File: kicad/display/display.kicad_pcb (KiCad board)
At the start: 2 copper layers, 190.5 x 38.1 mm, 27 parts, among them J10 Conn. 02x12, P1 10k, P2 10k, P3 10k stereo, P4 10k, T7 2N3904, T8 2N3904, U3 4066N

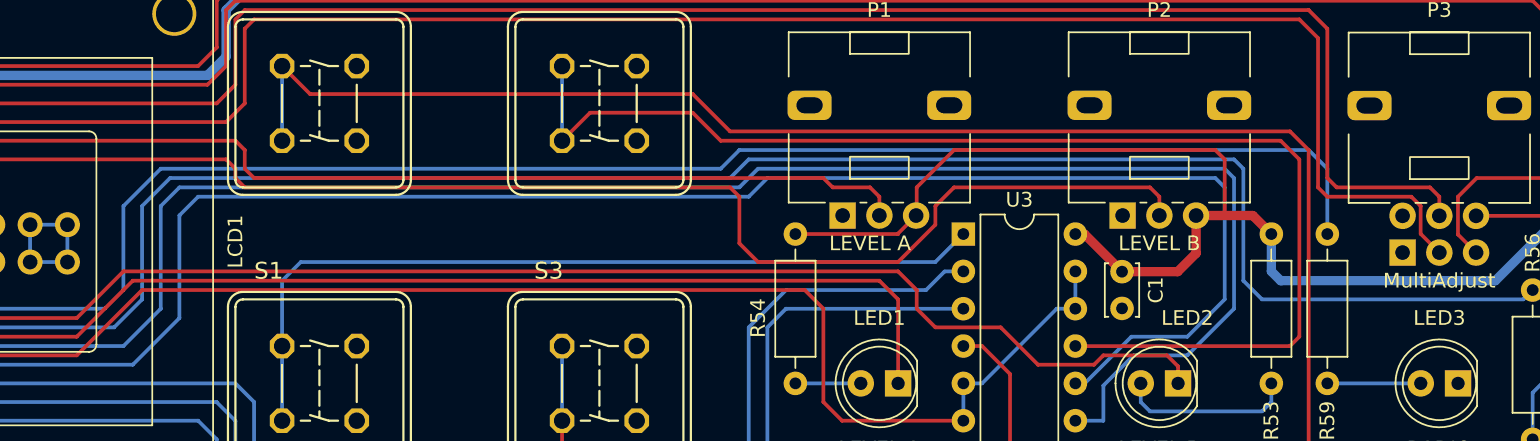
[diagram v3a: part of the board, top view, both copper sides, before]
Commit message: Cleaning up F.Fab layer, putting values at the right places.
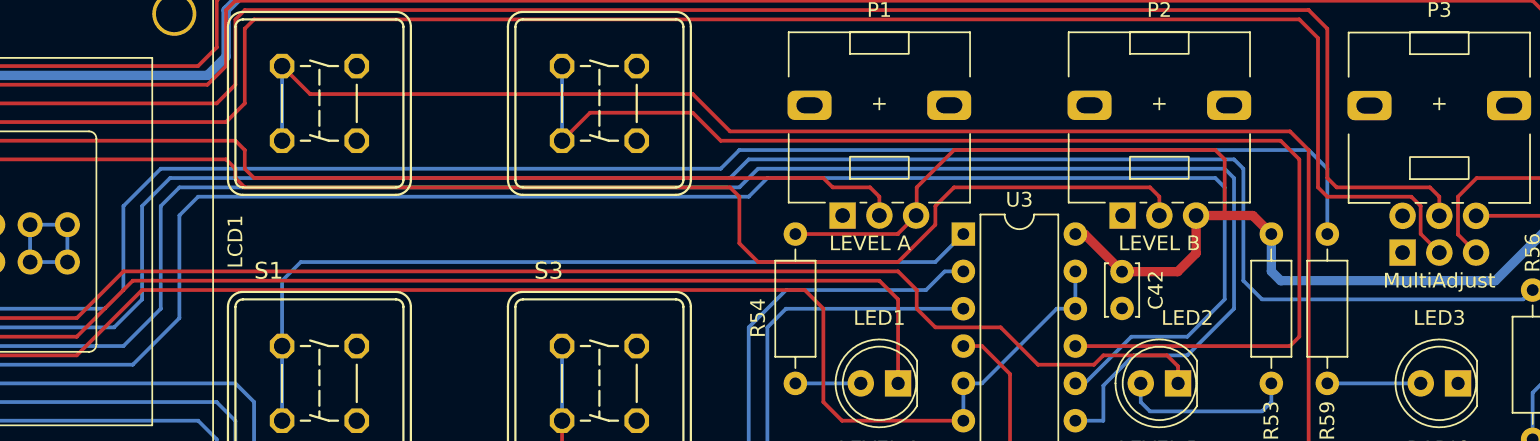
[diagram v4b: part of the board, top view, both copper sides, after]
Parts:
- renumbered C1 to C42
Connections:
- P1 pad MP: (no net) -> GND
- P2 pad MP: (no net) -> GND
- P3 pad MP: (no net) -> GND
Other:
- board text added: "+"
- board text removed: "16V"
- board text removed: "25V"
- board text removed: "6.3V"

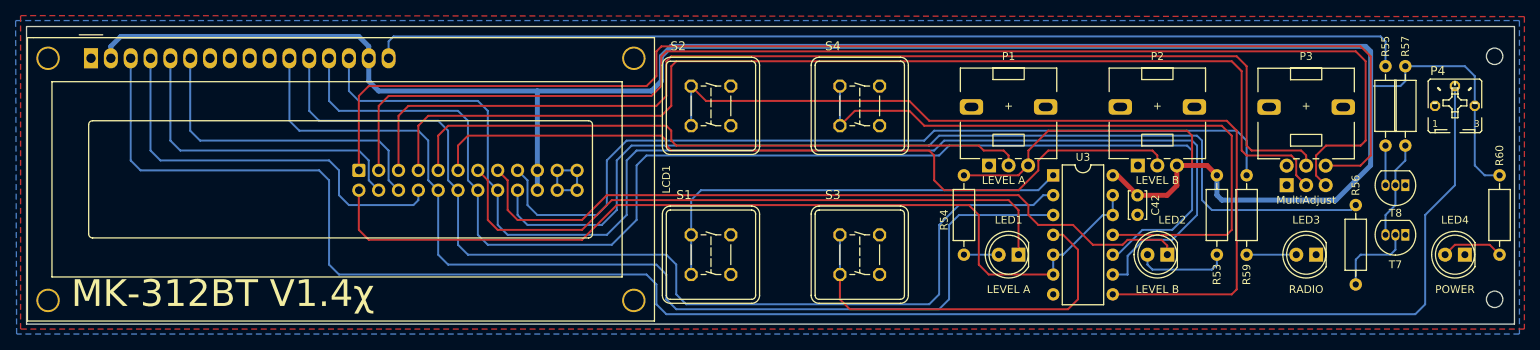
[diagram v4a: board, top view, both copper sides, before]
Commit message: Two small fixups for the display & frontend. Made mounting holes in display PCB larger. Moved LCD window slightly to the right on the front panel.
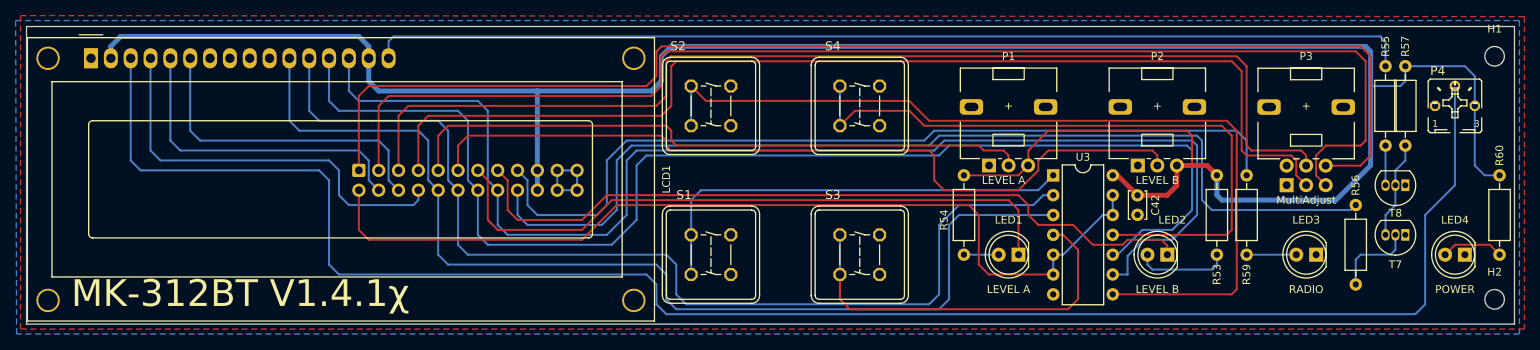
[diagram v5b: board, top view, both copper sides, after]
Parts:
- H1, H2: footprint MountingHole:MountingHole_2.1mm -> MountingHole:MountingHole_2.5mm
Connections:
- P1 pad MP: GND -> (no net)
- P2 pad MP: GND -> (no net)
- P3 pad MP: GND -> (no net)
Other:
- board text added: "MK-312BT V1.4.1χ"
- board text removed: "MK-312BT V1.4χ"
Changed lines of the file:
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@@
   (title_block
     (title "MK312BT Display Print")
-    (date "2022-08-01")
-    (rev "1.3.1-Chi")
+    (date "2022-09-05")
+    (rev "1.4.1-Chi")
   )
   (layers
@@
     )
   )
-  (footprint "MountingHole:MountingHole_2.1mm" (layer "F.Cu")
+  (footprint "MountingHole:MountingHole_2.5mm" (layer "F.Cu")
     (at 238.76 54.61)
-    (descr "Mounting Hole 2.1mm, no annular")
-    (tags "mounting hole 2.1mm no annular")
+    (descr "Mounting Hole 2.5mm, no annular")
+    (tags "mounting hole 2.5mm no annular")
     (property "Sheetfile" "display.kicad_sch")
     (property "Sheetname" "")
     (attr exclude_from_pos_files)
-    (fp_text reference "H1" (at 0 3.175) (layer "F.SilkS") hide
-      (effects (font (size 1 1) (thickness 0.15)))
-    )
-    (fp_text value "MountingHole topright" (at 0 3.2) (layer "F.Fab")
+    (fp_text reference "H1" (at 0 -3.5) (layer "F.SilkS")
+      (effects (font (size 1 1) (thickness 0.15)))
+    )
+    (fp_text value "MountingHole topright" (at 0 3.5) (layer "F.Fab") hide
       (effects (font (size 1 1) (thickness 0.15)))
     )
@@
       (effects (font (size 1 1) (thickness 0.15)))
     )
-    (fp_circle (center 0 0) (end 2.1 0) (layer "Cmts.User") (width 0.15) (fill none))
-    (fp_circle (center 0 0) (end 2.35 0) (layer "F.CrtYd") (width 0.05) (fill none))
-    (pad "" np_thru_hole circle (at 0 0) (size 2.1 2.1) (drill 2.1) (layers *.Cu *.Mask))
+    (fp_circle (center 0 0) (end 2.5 0) (layer "Cmts.User") (width 0.15) (fill none))
+    (fp_circle (center 0 0) (end 2.75 0) (layer "F.CrtYd") (width 0.05) (fill none))
+    (pad "" np_thru_hole circle (at 0 0) (size 2.5 2.5) (drill 2.5) (layers *.Cu *.Mask))
   )
   (footprint "Resistor_THT:R_Axial_DIN0207_L6.3mm_D2.5mm_P10.16mm_Horizontal" (layer "F.Cu")
@@
     (pad "3" thru_hole circle (at 0 5 90) (size 1.8 1.8) (drill 1) (layers *.Cu *.Mask)
       (net 27 "+5V") (pinfunction "3") (pintype "passive"))
-    (pad "MP" thru_hole roundrect (at 7.500011 7.249998 90) (size 2 2.999999) (drill oval 1.1 1.8) (layers *.Cu *.Mask) (roundrect_rratio 0.25)
-      (net 2 "GND"))
-    (pad "MP" thru_hole roundrect (at 7.500011 -2.250008 90) (size 2 2.999999) (drill oval 1.1 1.8) (layers *.Cu *.Mask) (roundrect_rratio 0.25)
-      (net 2 "GND"))
+    (pad "MP" thru_hole roundrect (at 7.500011 7.249998 90) (size 2 2.999999) (drill oval 1.1 1.8) (layers *.Cu *.Mask) (roundrect_rratio 0.25))
+    (pad "MP" thru_hole roundrect (at 7.500011 -2.250008 90) (size 2 2.999999) (drill oval 1.1 1.8) (layers *.Cu *.Mask) (roundrect_rratio 0.25))
     (zone (net 0) (net_name "") (layer "F.Cu") (name "Copper Keep Out") (hatch full 0.508)
       (connect_pads (clearance 0))
       (min_thickness 0.254)
-      (keepout (tracks not_allowed) (vias not_allowed) (pads not_allowed ) (copperpour not_allowed) (footprints not_allowed))
+      (keepout (tracks not_allowed) (vias not_allowed) (pads not_allowed) (copperpour not_allowed) (footprints not_allowed))
       (fill (thermal_gap 0.508) (thermal_bridge_width 0.508))
       (polygon
@@
       (connect_pads (clearance 0))
       (min_thickness 0.254)
-      (keepout (tracks not_allowed) (vias not_allowed) (pads not_allowed ) (copperpour not_allowed) (footprints not_allowed))
+      (keepout (tracks not_allowed) (vias not_allowed) (pads not_allowed) (copperpour not_allowed) (footprints not_allowed))
       (fill (thermal_gap 0.508) (thermal_bridge_width 0.508))
       (polygon
@@
     )
   )
-  (footprint "MountingHole:MountingHole_2.1mm" (layer "F.Cu")
+  (footprint "MountingHole:MountingHole_2.5mm" (layer "F.Cu")
     (at 238.76 85.725)
-    (descr "Mounting Hole 2.1mm, no annular")
-    (tags "mounting hole 2.1mm no annular")
+    (descr "Mounting Hole 2.5mm, no annular")
+    (tags "mounting hole 2.5mm no annular")
     (property "Sheetfile" "display.kicad_sch")
     (property "Sheetname" "")
     (attr exclude_from_pos_files)
-    (fp_text reference "H2" (at 0 -3.199994) (layer "F.SilkS") hide
-      (effects (font (size 1 1) (thickness 0.15)))
-    )
-    (fp_text value "MountingHole bottomright" (at 0 3.2) (layer "F.Fab")
+    (fp_text reference "H2" (at 0 -3.5) (layer "F.SilkS")
+      (effects (font (size 1 1) (thickness 0.15)))
+    )
+    (fp_text value "MountingHole bottomright" (at 0 3.5) (layer "F.Fab") hide
       (effects (font (size 1 1) (thickness 0.15)))
     )
@@
       (effects (font (size 1 1) (thickness 0.15)))
     )
-    (fp_circle (center 0 0) (end 2.1 0) (layer "Cmts.User") (width 0.15) (fill none))
-    (fp_circle (center 0 0) (end 2.35 0) (layer "F.CrtYd") (width 0.05) (fill none))
-    (pad "" np_thru_hole circle (at 0 0) (size 2.1 2.1) (drill 2.1) (layers *.Cu *.Mask))
+    (fp_circle (center 0 0) (end 2.5 0) (layer "Cmts.User") (width 0.15) (fill none))
+    (fp_circle (center 0 0) (end 2.75 0) (layer "F.CrtYd") (width 0.05) (fill none))
+    (pad "" np_thru_hole circle (at 0 0) (size 2.5 2.5) (drill 2.5) (layers *.Cu *.Mask))
   )
   (footprint "Potentiometer_THT:Potentiometer_Alps_RK09L_Double_Vertical" (layer "F.Cu")
@@
     (pad "6" thru_hole circle (at 2.5 5 90) (size 1.8 1.8) (drill 1) (layers *.Cu *.Mask)
       (net 1 "Net-(J10-Pad1)") (pinfunction "6") (pintype "passive"))
-    (pad "MP" thru_hole roundrect (at 10.000005 -2.250008 90) (size 2 2.999999) (drill oval 1.1 1.8) (layers *.Cu *.Mask) (roundrect_rratio 0.25)
-      (net 2 "GND"))
-    (pad "MP" thru_hole roundrect (at 10.000005 7.249998 90) (size 2 2.999999) (drill oval 1.1 1.8) (layers *.Cu *.Mask) (roundrect_rratio 0.25)
-      (net 2 "GND"))
+    (pad "MP" thru_hole roundrect (at 10.000005 -2.250008 90) (size 2 2.999999) (drill oval 1.1 1.8) (layers *.Cu *.Mask) (roundrect_rratio 0.25))
+    (pad "MP" thru_hole roundrect (at 10.000005 7.249998 90) (size 2 2.999999) (drill oval 1.1 1.8) (layers *.Cu *.Mask) (roundrect_rratio 0.25))
     (zone (net 0) (net_name "") (layer "F.Cu") (name "Copper Keep Out") (hatch full 0.508)
       (connect_pads (clearance 0))
       (min_thickness 0.254)
-      (keepout (tracks not_allowed) (vias not_allowed) (pads not_allowed ) (copperpour not_allowed) (footprints not_allowed))
+      (keepout (tracks not_allowed) (vias not_allowed) (pads not_allowed) (copperpour not_allowed) (footprints not_allowed))
       (fill (thermal_gap 0.508) (thermal_bridge_width 0.508))
       (polygon
@@
       (connect_pads (clearance 0))
       (min_thickness 0.254)
-      (keepout (tracks not_allowed) (vias not_allowed) (pads not_allowed ) (copperpour not_allowed) (footprints not_allowed))
+      (keepout (tracks not_allowed) (vias not_allowed) (pads not_allowed) (copperpour not_allowed) (footprints not_allowed))
       (fill (thermal_gap 0.508) (thermal_bridge_width 0.508))
       (polygon
@@
     (pad "3" thru_hole circle (at 0 5 90) (size 1.8 1.8) (drill 1) (layers *.Cu *.Mask)
       (net 27 "+5V") (pinfunction "3") (pintype "passive"))
-    (pad "MP" thru_hole roundrect (at 7.500011 7.249998 90) (size 2 2.999999) (drill oval 1.1 1.8) (layers *.Cu *.Mask) (roundrect_rratio 0.25)
-      (net 2 "GND"))
-    (pad "MP" thru_hole roundrect (at 7.500011 -2.250008 90) (size 2 2.999999) (drill oval 1.1 1.8) (layers *.Cu *.Mask) (roundrect_rratio 0.25)
-      (net 2 "GND"))
+    (pad "MP" thru_hole roundrect (at 7.500011 7.249998 90) (size 2 2.999999) (drill oval 1.1 1.8) (layers *.Cu *.Mask) (roundrect_rratio 0.25))
+    (pad "MP" thru_hole roundrect (at 7.500011 -2.250008 90) (size 2 2.999999) (drill oval 1.1 1.8) (layers *.Cu *.Mask) (roundrect_rratio 0.25))
     (zone (net 0) (net_name "") (layer "F.Cu") (name "Copper Keep Out") (hatch full 0.508)
       (connect_pads (clearance 0))
       (min_thickness 0.254)
-      (keepout (tracks not_allowed) (vias not_allowed) (pads not_allowed ) (copperpour not_allowed) (footprints not_allowed))
+      (keepout (tracks not_allowed) (vias not_allowed) (pads not_allowed) (copperpour not_allowed) (footprints not_allowed))
       (fill (thermal_gap 0.508) (thermal_bridge_width 0.508))
       (polygon
@@
       (connect_pads (clearance 0))
       (min_thickness 0.254)
-      (keepout (tracks not_allowed) (vias not_allowed) (pads not_allowed ) (copperpour not_allowed) (footprints not_allowed))
+      (keepout (tracks not_allowed) (vias not_allowed) (pads not_allowed) (copperpour not_allowed) (footprints not_allowed))
       (fill (thermal_gap 0.508) (thermal_bridge_width 0.508))
       (polygon
@@
       (effects (font (size 1 1) (thickness 0.15)))
     )
-    (fp_text value "RC1602A" (at -4.31 34.66) (layer "F.Fab")
+    (fp_text value "RC1602A" (at 11.43 17.526) (layer "F.Fab")
       (effects (font (size 1 1) (thickness 0.15)))
     )
@@
     (fp_arc (start -0.29972 8.49884) (mid -0.153162 8.145018) (end 0.20066 7.99846) (layer "F.SilkS") (width 0.12))
     (fp_arc (start 63.7 8) (mid 64.053553 8.146447) (end 64.2 8.5) (layer "F.SilkS") (width 0.12))
-    (fp_arc (start 64.20104 22.49932) (mid 64.054479 22.85315) (end 63.70066 22.9997) (layer "F.SilkS") (width 0.12))
+    (fp_arc (start 64.20104 22.49932) (mid 64.054473 22.853115) (end 63.70066 22.9997) (layer "F.SilkS") (width 0.12))
     (fp_arc (start 0.20066 22.9997) (mid -0.153162 22.853142) (end -0.29972 22.49932) (layer "F.SilkS") (width 0.12))
     (fp_line (start -8.25 -2.75) (end 72.25 -2.75) (layer "F.CrtYd") (width 0.05))
@@
   (gr_line (start 241.3 50.8) (end 50.8 50.8) (layer "Edge.Cuts") (width 0.05))
   (gr_line (start 241.3 88.9) (end 241.3 50.8) (layer "Edge.Cuts") (width 0.05))
-  (gr_text "MK-312BT V1.4χ" (at 56.515 86.995) (layer "F.SilkS")
+  (gr_text "MK-312BT V1.4.1χ" (at 56.515 86.995) (layer "F.SilkS")
     (effects (font (size 3.429 3.429) (thickness 0.381)) (justify left bottom))
   )
